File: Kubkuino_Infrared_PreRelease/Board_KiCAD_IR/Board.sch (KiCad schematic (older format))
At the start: 31 parts, among them J1 Piezo, J2 Conn_01x03, J3 I2C, J4 Conn_01x03, J6 AC/DC In (12V), J7 Bluetooth, J8 Button, Q1 S8050, U1 ATMEGA328P-AU, U2 LM7805_TO220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

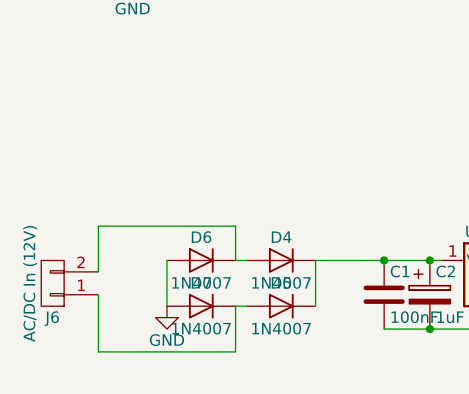
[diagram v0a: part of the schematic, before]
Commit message: cleaning, organizing
added DEBUG option during compilation
splashscreen
parts with prices (PL)
slight board changes
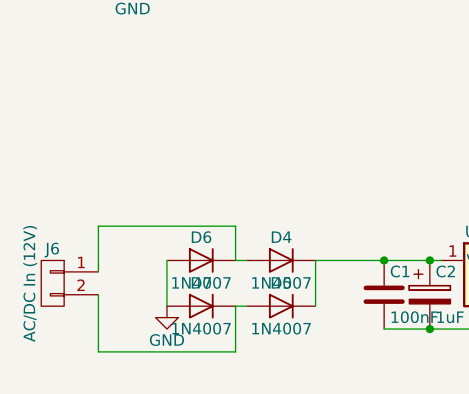
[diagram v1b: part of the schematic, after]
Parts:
- U2: footprint TO_SOT_Packages_SMD:TO-263-2 -> TO_SOT_Packages_SMD:TO-252-2
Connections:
- net at D4.2 (A), D6.1 (K): now also J6.1 (P1); no longer J6.2 (P2)
- net at D5.2 (A), D7.1 (K): now also J6.2 (P2); no longer J6.1 (P1)
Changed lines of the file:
@@
-EESchema Schematic File Version 2
+EESchema Schematic File Version 3
 LIBS:power
 LIBS:device
@@
 LIBS:ftdi
 LIBS:gennum
+LIBS:graphic
 LIBS:graphic_symbols
 LIBS:hc11
@@
 F 0 "U2" H 4300 5375 50  0000 C CNN
 F 1 "LM7805_TO220" H 4450 5375 50  0000 L CNN
-F 2 "TO_SOT_Packages_SMD:TO-263-2" H 4450 5475 50  0001 C CIN
+F 2 "TO_SOT_Packages_SMD:TO-252-2" H 4450 5475 50  0001 C CIN
 F 3 "" H 4450 5200 50  0001 C CNN
 	1    4450 5250
@@
 F 3 "" H 2450 5350 50  0001 C CNN
 	1    2450 5350
-	-1   0    0    1
+	-1   0    0    -1
 $EndComp
 Text GLabel 5450 5250 2    60   Input ~ 0

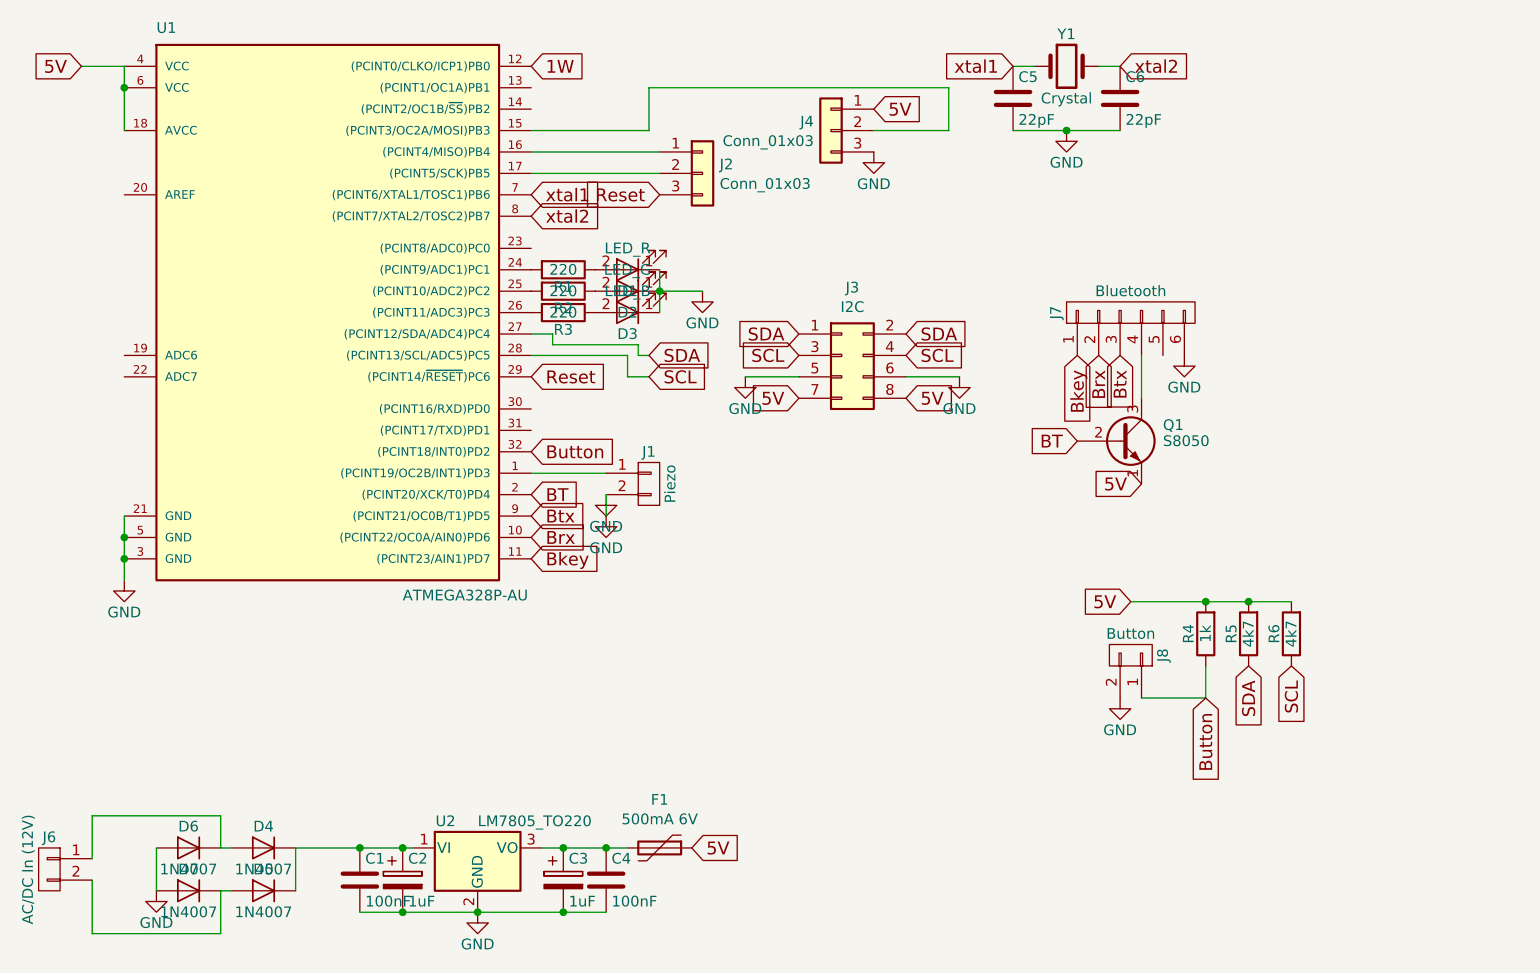
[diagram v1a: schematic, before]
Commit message: Updates
Finished new board
Changed SSD1306 to 128x64
Major RAM optimization
Main routine optimizations
Set up display layout
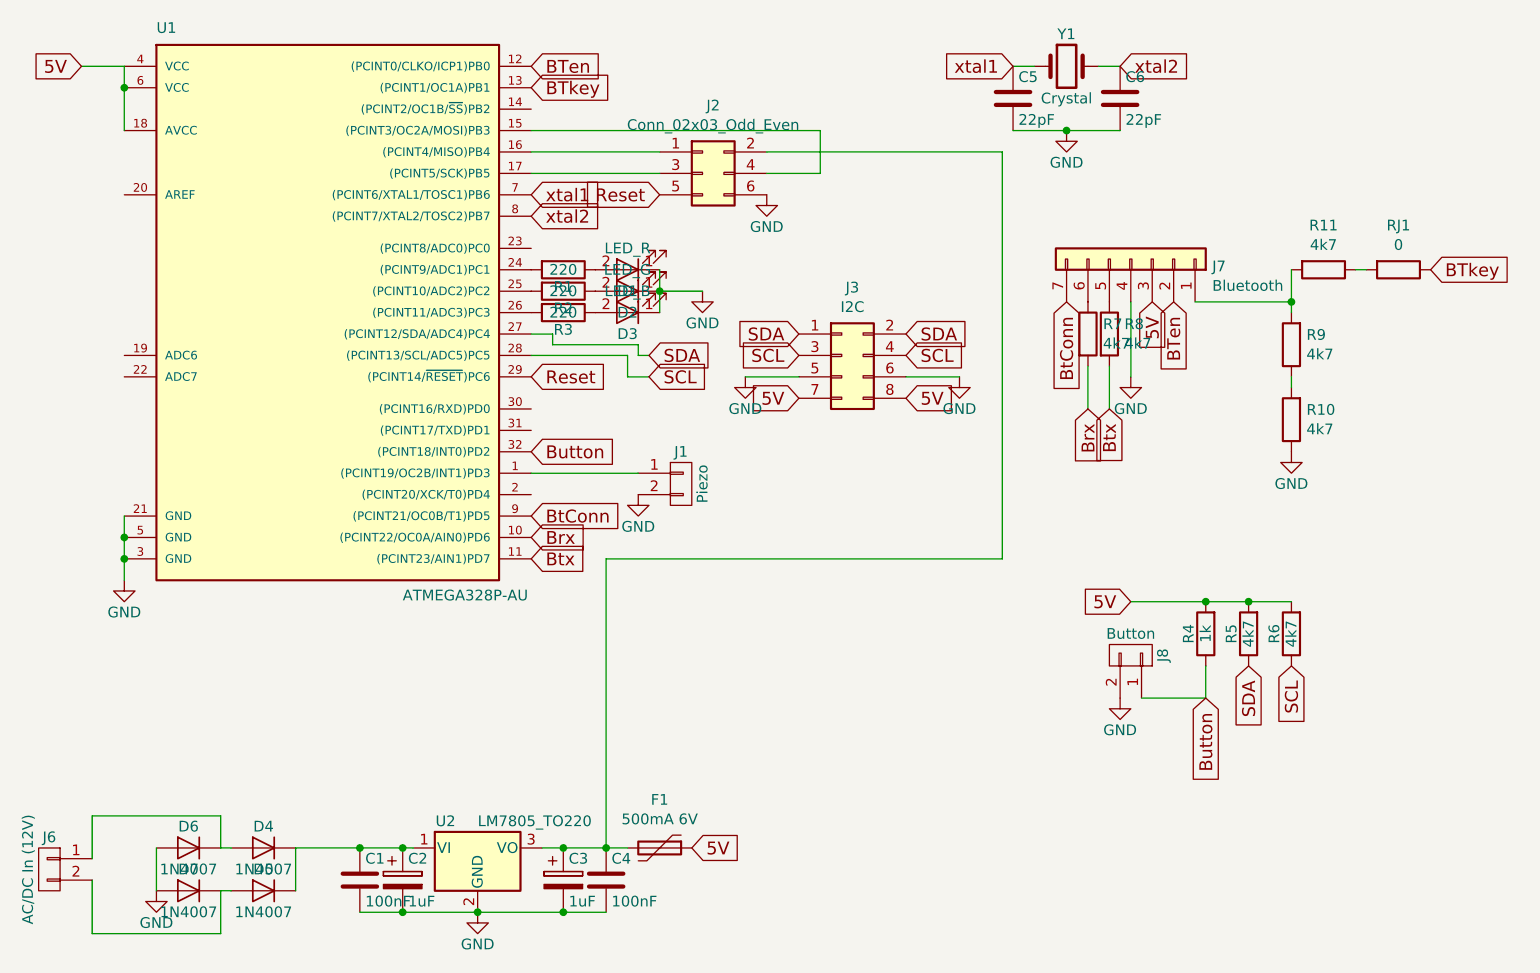
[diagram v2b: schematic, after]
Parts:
- removed J2, J4: Conn_01x03, Socket_Strips:Socket_Strip_Straight_1x03_Pitch2.54mm, symbol Conn_01x03
- removed J7: Bluetooth, Pin_Headers:Pin_Header_Straight_1x06_Pitch2.54mm_SMD_Pin1Left, symbol CONN_01X06
- removed Q1: S8050, TO_SOT_Packages_THT:TO-92_Inline_Wide, symbol S8050
- added J2: Conn_02x03_Odd_Even, Pin_Headers:Pin_Header_Straight_2x03_Pitch2.54mm, symbol Conn_02x03_Odd_Even
- added J7: Bluetooth, Pin_Headers:Pin_Header_Straight_1x07_Pitch2.54mm_SMD_Pin1Left, symbol Conn_01x07
- added R10, R11, R7, R8, R9: 4k7, Resistors_SMD:R_1206, symbol R
- added RJ1: 0, Resistors_SMD:R_1206, symbol R
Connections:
- net Bkey is gone; now on net Btx: U1.11 ((PCINT23/AIN1)PD7)
- net 5V: now also J7.3 (Pin_3)
- net Brx: now also R7.2
- net Btx: now also R8.2; no longer U1.9 ((PCINT21/OC0B/T1)PD5)
- net GND: now also J2.6 (Pin_6), J7.4 (Pin_4), R10.1
- net Reset: now also J2.5 (Pin_5)
- net at C3.1, C4.1, F1.2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: now also J2.2 (Pin_2)
- net BTkey: now reaches U1.13 ((PCINT1/OC1A)PB1)
- net BTkey: now also RJ1.1
- net at U1.15 ((PCINT3/OC2A/MOSI)PB3): now also J2.4 (Pin_4)
- net at U1.16 ((PCINT4/MISO)PB4): now also J2.1 (Pin_1)
- net at U1.17 ((PCINT5/SCK)PB5): now also J2.3 (Pin_3)
- net 1W renamed BTen
- net BTen: now also J7.2 (Pin_2)
- net BT: no longer names the net of U1.2 ((PCINT20/XCK/T0)PD4)
- new net: J7.1 (Pin_1), R11.2, R9.2
- new net: J7.5 (Pin_5), R8.1
- new net: J7.6 (Pin_6), R7.1
- new net: R11.1, RJ1.2
- new net: R10.2, R9.1
- new net BtConn: J7.7 (Pin_7), U1.9 ((PCINT21/OC0B/T1)PD5)
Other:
- moved on the sheet: J1
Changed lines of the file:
@@
 Text GLabel 2600 1600 0    60   Input ~ 0
 5V
-$Comp
-L GND #PWR04
-U 1 1 5974A6F8
-P 5050 3700
-F 0 "#PWR04" H 5050 3450 50  0001 C CNN
-F 1 "GND" H 5050 3550 50  0000 C CNN
-F 2 "" H 5050 3700 50  0001 C CNN
-F 3 "" H 5050 3700 50  0001 C CNN
-	1    5050 3700
-	1    0    0    -1
-$EndComp
 Text GLabel 7500 4100 0    60   Input ~ 0
 5V
@@
 L CONN_01X02 J1
 U 1 1 59750D8D
-P 5250 3550
-F 0 "J1" H 5250 3700 50  0000 C CNN
-F 1 "Piezo" V 5350 3550 50  0000 C CNN
-F 2 "Pin_Headers:Pin_Header_Straight_1x02_Pitch2.54mm_SMD_Pin1Left" H 5250 3550 50  0001 C CNN
-F 3 "" H 5250 3550 50  0001 C CNN
-	1    5250 3550
-	1    0    0    -1
-$EndComp
-$Comp
-L GND #PWR03
-U 1 1 59751385
-P 5050 3600
-F 0 "#PWR03" H 5050 3350 50  0001 C CNN
-F 1 "GND" H 5050 3450 50  0000 C CNN
-F 2 "" H 5050 3600 50  0001 C CNN
-F 3 "" H 5050 3600 50  0001 C CNN
-	1    5050 3600
+P 5400 3550
+F 0 "J1" H 5400 3700 50  0000 C CNN
+F 1 "Piezo" V 5500 3550 50  0000 C CNN
+F 2 "Pin_Headers:Pin_Header_Straight_1x02_Pitch2.54mm_SMD_Pin1Left" H 5400 3550 50  0001 C CNN
+F 3 "" H 5400 3550 50  0001 C CNN
+	1    5400 3550
 	1    0    0    -1
 $EndComp
@@
 L GND #PWR011
 U 1 1 59752C5D
-P 7750 2950
-F 0 "#PWR011" H 7750 2700 50  0001 C CNN
-F 1 "GND" H 7750 2800 50  0000 C CNN
-F 2 "" H 7750 2950 50  0001 C CNN
-F 3 "" H 7750 2950 50  0001 C CNN
-	1    7750 2950
-	1    0    0    -1
-$EndComp
-$Comp
-L S8050 Q1
-U 1 1 5975351B
-P 7450 3350
-F 0 "Q1" H 7650 3425 50  0000 L CNN
-F 1 "S8050" H 7650 3350 50  0000 L CNN
-F 2 "TO_SOT_Packages_THT:TO-92_Inline_Wide" H 7650 3275 50  0001 L CIN
-F 3 "" H 7450 3350 50  0001 L CNN
-	1    7450 3350
-	1    0    0    -1
-$EndComp
-Text GLabel 7250 3350 0    60   Input ~ 0
-BT
-Text GLabel 7550 3550 0    60   Input ~ 0
+P 7500 3050
+F 0 "#PWR011" H 7500 2800 50  0001 C CNN
+F 1 "GND" H 7500 2900 50  0000 C CNN
+F 2 "" H 7500 3050 50  0001 C CNN
+F 3 "" H 7500 3050 50  0001 C CNN
+	1    7500 3050
+	1    0    0    -1
+$EndComp
+Text GLabel 7700 2700 3    60   Input ~ 0
+BTen
+Text GLabel 7600 2700 3    60   Input ~ 0
 5V
-Text GLabel 4700 3700 2    60   Input ~ 0
+Text GLabel 4700 3900 2    60   Input ~ 0
 Btx
 Text GLabel 4700 3800 2    60   Input ~ 0
 Brx
-Text GLabel 7450 2950 3    60   Input ~ 0
+Text GLabel 7400 3200 3    60   Input ~ 0
 Btx
-Text GLabel 7350 2950 3    60   Input ~ 0
+Text GLabel 7300 3200 3    60   Input ~ 0
 Brx
-Text GLabel 4700 3900 2    60   Input ~ 0
-Bkey
-$Comp
-L CONN_01X06 J7
-U 1 1 59754103
-P 7500 2750
-F 0 "J7" H 7500 3100 50  0000 C CNN
-F 1 "Bluetooth" V 7600 2750 50  0000 C CNN
-F 2 "Pin_Headers:Pin_Header_Straight_1x06_Pitch2.54mm_SMD_Pin1Left" H 7500 2750 50  0001 C CNN
-F 3 "" H 7500 2750 50  0001 C CNN
-	1    7500 2750
-	0    -1   -1   0
-$EndComp
-Text GLabel 7250 2950 3    60   Input ~ 0
-Bkey
 $Comp
 L GND #PWR06
@@
 L GND #PWR08
 U 1 1 59757B5E
-P 6300 2000
-F 0 "#PWR08" H 6300 1750 50  0001 C CNN
-F 1 "GND" H 6300 1850 50  0000 C CNN
-F 2 "" H 6300 2000 50  0001 C CNN
-F 3 "" H 6300 2000 50  0001 C CNN
-	1    6300 2000
-	1    0    0    -1
-$EndComp
-Text GLabel 6300 1800 2    60   Input ~ 0
-5V
-Text GLabel 4700 1600 2    60   Input ~ 0
-1W
+P 5800 2200
+F 0 "#PWR08" H 5800 1950 50  0001 C CNN
+F 1 "GND" H 5800 2050 50  0000 C CNN
+F 2 "" H 5800 2200 50  0001 C CNN
+F 3 "" H 5800 2200 50  0001 C CNN
+	1    5800 2200
+	1    0    0    -1
+$EndComp
 Text GLabel 6450 2850 2    60   Input ~ 0
 SDA
 Text GLabel 6450 2950 2    60   Input ~ 0
 SCL
-Text GLabel 4700 3600 2    60   Input ~ 0
-BT
+Text GLabel 4700 1600 2    60   Input ~ 0
+BTen
 $Comp
 L D D4
@@
 	1    0    0    -1
 $EndComp
-$Comp
-L Conn_01x03 J2
-U 1 1 59DD551F
-P 5500 2100
-F 0 "J2" H 5580 2142 50  0000 L CNN
-F 1 "Conn_01x03" H 5580 2051 50  0000 L CNN
-F 2 "Socket_Strips:Socket_Strip_Straight_1x03_Pitch2.54mm" H 5500 2100 50  0001 C CNN
-F 3 "" H 5500 2100 50  0001 C CNN
-	1    5500 2100
-	1    0    0    -1
-$EndComp
-$Comp
-L Conn_01x03 J4
-U 1 1 59DD580E
-P 6100 1900
-F 0 "J4" H 6180 1942 50  0000 L CNN
-F 1 "Conn_01x03" H 6180 1851 50  0000 L CNN
-F 2 "Socket_Strips:Socket_Strip_Straight_1x03_Pitch2.54mm" H 6100 1900 50  0001 C CNN
-F 3 "" H 6100 1900 50  0001 C CNN
-	1    6100 1900
-	-1   0    0    -1
-$EndComp
 Connection ~ 7850 4100
 Wire Wire Line
 	7500 4100 8250 4100
-Wire Wire Line
-	6650 1900 6300 1900
-Wire Wire Line
-	6650 1700 6650 1900
 Wire Wire Line
 	4700 2100 5300 2100
@@
 Wire Wire Line
 	2650 5650 2650 5400
-Wire Wire Line
-	5050 3600 5050 3700
 Connection ~ 8050 4100
 Wire Wire Line
@@
 	5300 2650 5500 2650
 Connection ~ 5300 2650
-Wire Wire Line
-	4700 3500 5050 3500
-Wire Wire Line
-	7550 2950 7550 3150
 Wire Wire Line
 	3900 5550 5050 5550
@@
 Wire Wire Line
 	6950 1900 7450 1900
-Wire Wire Line
-	5250 1900 4700 1900
-Wire Wire Line
-	5250 1700 5250 1900
-Wire Wire Line
-	5250 1700 6650 1700
 Wire Wire Line
 	3600 5250 3600 5450
@@
 	1    0    0    -1
 $EndComp
+Text GLabel 4700 3700 2    60   Input ~ 0
+BtConn
+Text GLabel 7200 2700 3    60   Input ~ 0
+BtConn
+Wire Wire Line
+	4700 3500 5200 3500
+$Comp
+L GND #PWR03
+U 1 1 5A033977
+P 5200 3600
+F 0 "#PWR03" H 5200 3350 50  0001 C CNN
+F 1 "GND" H 5200 3450 50  0000 C CNN
+F 2 "" H 5200 3600 50  0001 C CNN
+F 3 "" H 5200 3600 50  0001 C CNN
+	1    5200 3600
+	1    0    0    -1
+$EndComp
+$Comp
+L Conn_02x03_Odd_Even J2
+U 1 1 5A035BE6
+P 5500 2100
+F 0 "J2" H 5550 2417 50  0000 C CNN
+F 1 "Conn_02x03_Odd_Even" H 5550 2326 50  0000 C CNN
+F 2 "Pin_Headers:Pin_Header_Straight_2x03_Pitch2.54mm" H 5500 2100 50  0001 C CNN
+F 3 "~" H 5500 2100 50  0001 C CNN
+	1    5500 2100
+	1    0    0    -1
+$EndComp
+Wire Wire Line
+	4700 1900 6050 1900
+Wire Wire Line
+	6050 1900 6050 2100
+Wire Wire Line
+	6050 2100 5800 2100
+Text GLabel 4700 1700 2    60   Input ~ 0
+BTkey
+$Comp
+L Conn_01x07 J7
+U 1 1 5A0496ED
+P 7500 2500
+F 0 "J7" V 7466 2880 50  0000 L CNN
+F 1 "Bluetooth" V 7375 2880 50  0000 L CNN
+F 2 "Pin_Headers:Pin_Header_Straight_1x07_Pitch2.54mm_SMD_Pin1Left" H 7500 2500 50  0001 C CNN
+F 3 "~" H 7500 2500 50  0001 C CNN
+	1    7500 2500
+	0    1    -1   0
+$EndComp
+Text GLabel 8900 2550 2    60   Input ~ 0
+BTkey
+$Comp
+L R R7
+U 1 1 5A04A4D2
+P 7300 2850
+F 0 "R7" H 7370 2896 50  0000 L CNN
+F 1 "4k7" H 7370 2805 50  0000 L CNN
+F 2 "Resistors_SMD:R_1206" V 7230 2850 50  0001 C CNN
+F 3 "" H 7300 2850 50  0001 C CNN
+	1    7300 2850
+	1    0    0    -1
+$EndComp
+$Comp
+L R R8
+U 1 1 5A04A6EB
+P 7400 2850
+F 0 "R8" H 7470 2896 50  0000 L CNN
+F 1 "4k7" H 7470 2805 50  0000 L CNN
+F 2 "Resistors_SMD:R_1206" V 7330 2850 50  0001 C CNN
+F 3 "" H 7400 2850 50  0001 C CNN
+	1    7400 2850
+	1    0    0    -1
+$EndComp
+Wire Wire Line
+	7400 3200 7400 3000
+Wire Wire Line
+	7300 3000 7300 3200
+Wire Wire Line
+	7500 3050 7500 2700
+$Comp
+L R R11
+U 1 1 5A04BE79
+P 8400 2550
+F 0 "R11" V 8193 2550 50  0000 C CNN
+F 1 "4k7" V 8284 2550 50  0000 C CNN
+F 2 "Resistors_SMD:R_1206" V 8330 2550 50  0001 C CNN
+F 3 "" H 8400 2550 50  0001 C CNN
+	1    8400 2550
+	0    1    1    0
+$EndComp
+Wire Wire Line
+	8250 2550 8250 2750
+Wire Wire Line
+	8250 2700 7800 2700
+Connection ~ 8250 2700
+Wire Wire Line
+	8250 3100 8250 3050
+$Comp
+L GND #PWR04
+U 1 1 5A04C33C
+P 8250 3400
+F 0 "#PWR04" H 8250 3150 50  0001 C CNN
+F 1 "GND" H 8250 3250 50  0000 C CNN
+F 2 "" H 8250 3400 50  0001 C CNN
+F 3 "" H 8250 3400 50  0001 C CNN
+	1    8250 3400
+	1    0    0    -1
+$EndComp
+$Comp
+L R R9
+U 1 1 5A04C569
+P 8250 2900
+F 0 "R9" H 8180 2854 50  0000 R CNN
+F 1 "4k7" H 8180 2945 50  0000 R CNN
+F 2 "Resistors_SMD:R_1206" V 8180 2900 50  0001 C CNN
+F 3 "" H 8250 2900 50  0001 C CNN
+	1    8250 2900
+	-1   0    0    1
+$EndComp
+$Comp
+L R R10
+U 1 1 5A04C5F1
+P 8250 3250
+F 0 "R10" H 8180 3204 50  0000 R CNN
+F 1 "4k7" H 8180 3295 50  0000 R CNN
+F 2 "Resistors_SMD:R_1206" V 8180 3250 50  0001 C CNN
+F 3 "" H 8250 3250 50  0001 C CNN
+	1    8250 3250
+	-1   0    0    1
+$EndComp
+$Comp
+L R RJ1
+U 1 1 5A04D77F
+P 8750 2550
+F 0 "RJ1" V 8543 2550 50  0000 C CNN
+F 1 "0" V 8634 2550 50  0000 C CNN
+F 2 "Resistors_SMD:R_1206" V 8680 2550 50  0001 C CNN
+F 3 "" H 8750 2550 50  0001 C CNN
+	1    8750 2550
+	0    1    1    0
+$EndComp
+Wire Wire Line
+	8550 2550 8600 2550
+Wire Wire Line
+	5050 5250 5050 3900
+Wire Wire Line
+	5050 3900 6900 3900
+Wire Wire Line
+	6900 3900 6900 2000
+Wire Wire Line
+	6900 2000 5800 2000
 $EndSCHEMATC
